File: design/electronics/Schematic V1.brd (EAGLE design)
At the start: 152.4 x 139.7 mm, 180 parts, among them J1 PJ-202AH, J2 PJ-025, J3 DD50P564GTXLF, J4 DD50P564GTXLF, J5 SAMTEC-TST-105-01-X-DJ, J6 SSW-106-02-TM-S-RA, SW1 TL6330AF200Q, U1 STM32F207VGT6TR, U10 SN65LBC175ADD16-M, U11 MAX7375AXR805+T21-0075D_MXM-M, U12 SN75ALS174ADWRDW20-M, U13 SN75468DRD0016A_M, U14 SN75468DRD0016A_M, U15 ACSL-6400-00TESOIC_6400-00TE-M, U16 ACSL-6400-00TESOIC_6400-00TE-M, U17 SN65LBC175ADD16-M, U18 SN65LBC175ADD16-M, U19 SN65LBC175ADD16-M, U2 LM2678S-5.0/NOPBTS7B-M, U21 RS0104YQTSSOP-14_JRT-M, U22 RS0104YQTSSOP-14_JRT-M, U24 RS0104YQTSSOP-14_JRT-M, U3 CDBC520-GCDBC-G-M, U4 TLV1117LV33DCYR, U5 LM43601PWPRPWP16_TEX-M, U6 RS0104YQTSSOP-14_JRT-M, U7 SN75ALS174ADWRDW20-M, U8 OPA4205APWRTSSOP14_PW_R-PDSO-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

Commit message: Yay it's hooked up
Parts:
- added R75: 33k, rcl:R0805
- added R76: 66k, rcl:R0805
- moved LED3 143.4 mm to (42.5, 54.6), turned to 270 degrees
- moved LED4 113.1 mm to (3.81, 66.0), turned to 180 degrees
- moved TP5 106.0 mm to (50.8, 130.8)
- moved TP6 97.8 mm to (58.4, 69.8)
- moved TP4 90.9 mm to (34.3, 130.8)
- moved TP3 86.0 mm to (50.8, 47.0)
- moved TP2 67.5 mm to (37.5, 60.7)
- moved R21 58.0 mm to (41.5, 58.4), turned to 270 degrees
- moved R22 29.0 mm to (3.81, 71.1), turned to 270 degrees
- moved R73 0.28 mm to (68.1, 105.4)
- moved C53 0.28 mm to (115.4, 25.1)
- renumbered U10 to LINE_RECEIVER, U13 to NPN, U15 to OPTOCOUPLER, U21 to LEVEL_SHIFTER
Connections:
- removed net V_ON_5V: U12.15
- new net V_ON_5V_6: R75.1, R76.2, U12.15
- net +5V: now also R75.2
- net S_GND: now also R76.1
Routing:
- net TORQUE-SPEED_ANALOG_2: track 8.11 -> 149.9 mm, vias 1 -> 7
- net P_GND: track 231.1 -> 319.1 mm, vias 19 -> 27
- net S_GND: track 495.2 -> 513.9 mm, vias 34 -> 36
- net +5V: track 320.8 -> 333.8 mm, vias 21 -> 24
- net +3.3V: track 227.5 -> 238.7 mm, vias 19 -> 21
- net V_ON_5V_6: track 0.00 -> 9.01 mm, vias 0 -> 1
- net N$30: track 0.00 -> 3.08 mm
- net N$24: track 0.00 -> 2.85 mm
- net SERVO_ALARM_OUT_LO_1: track 32.3 -> 34.5 mm
- net +24V: track 447.8 -> 449.5 mm
- net ALO_GPIO_A_1: track 17.1 -> 15.5 mm
- net V_ON_14V: track 6.39 -> 7.86 mm
- net ENC_PUL_OUT_C_LO_2: track 31.7 -> 30.9 mm
- net CLR_LO_2: track 92.5 -> 93.3 mm
- net ALO_GPIO_C_2: track 36.4 -> 35.7 mm
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
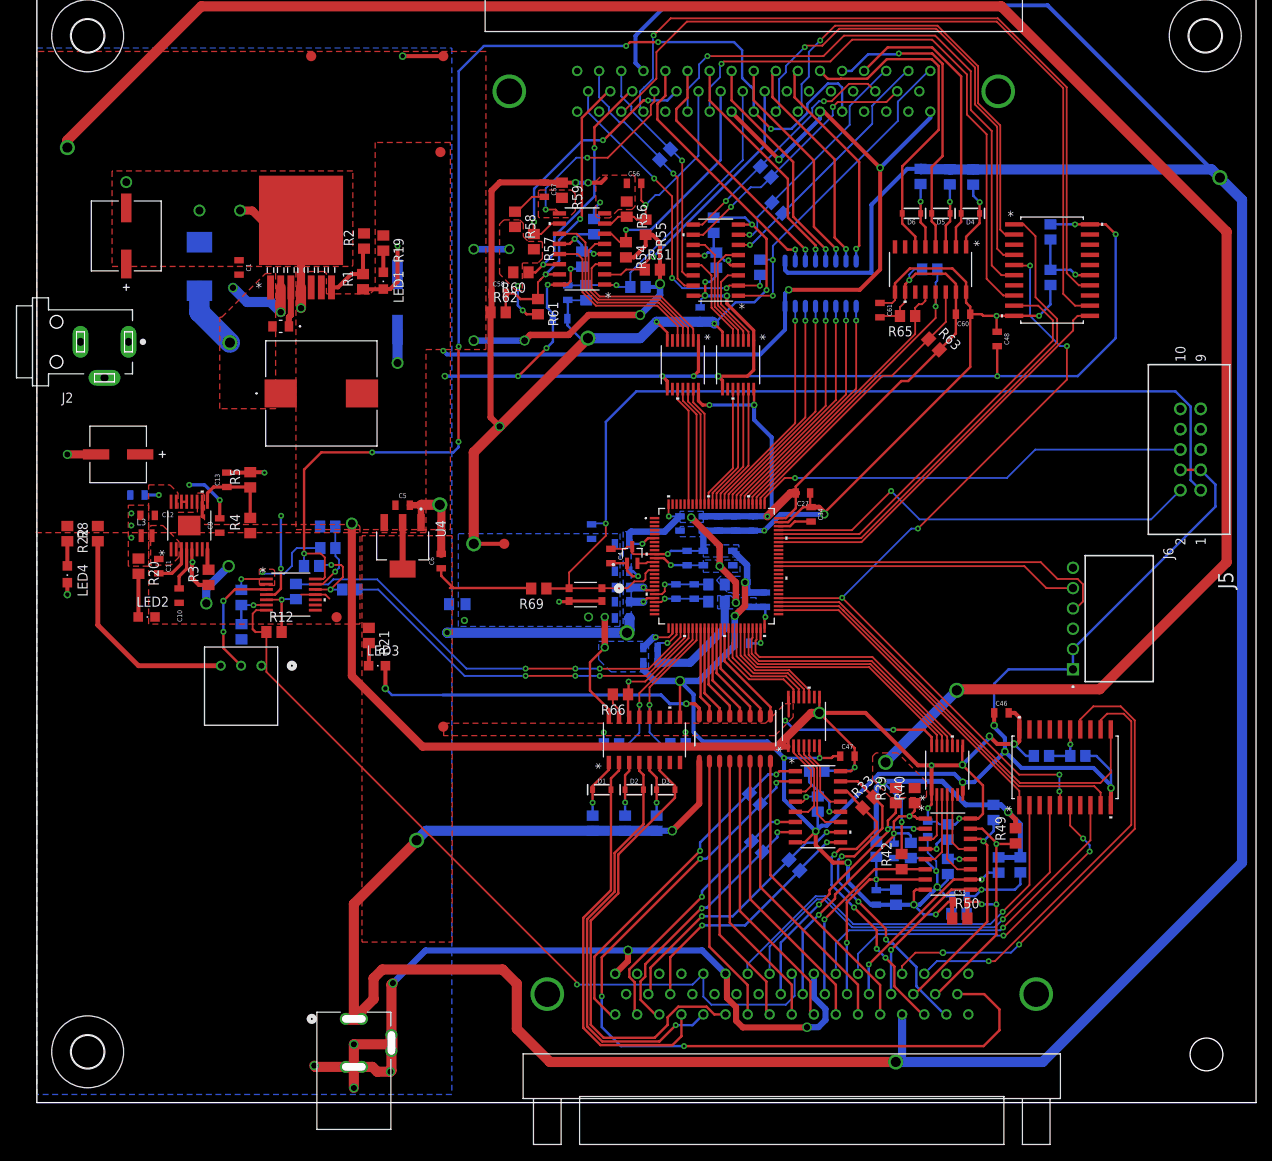
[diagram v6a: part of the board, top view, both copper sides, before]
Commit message: Updated part library of barrel jack + stretched polygons
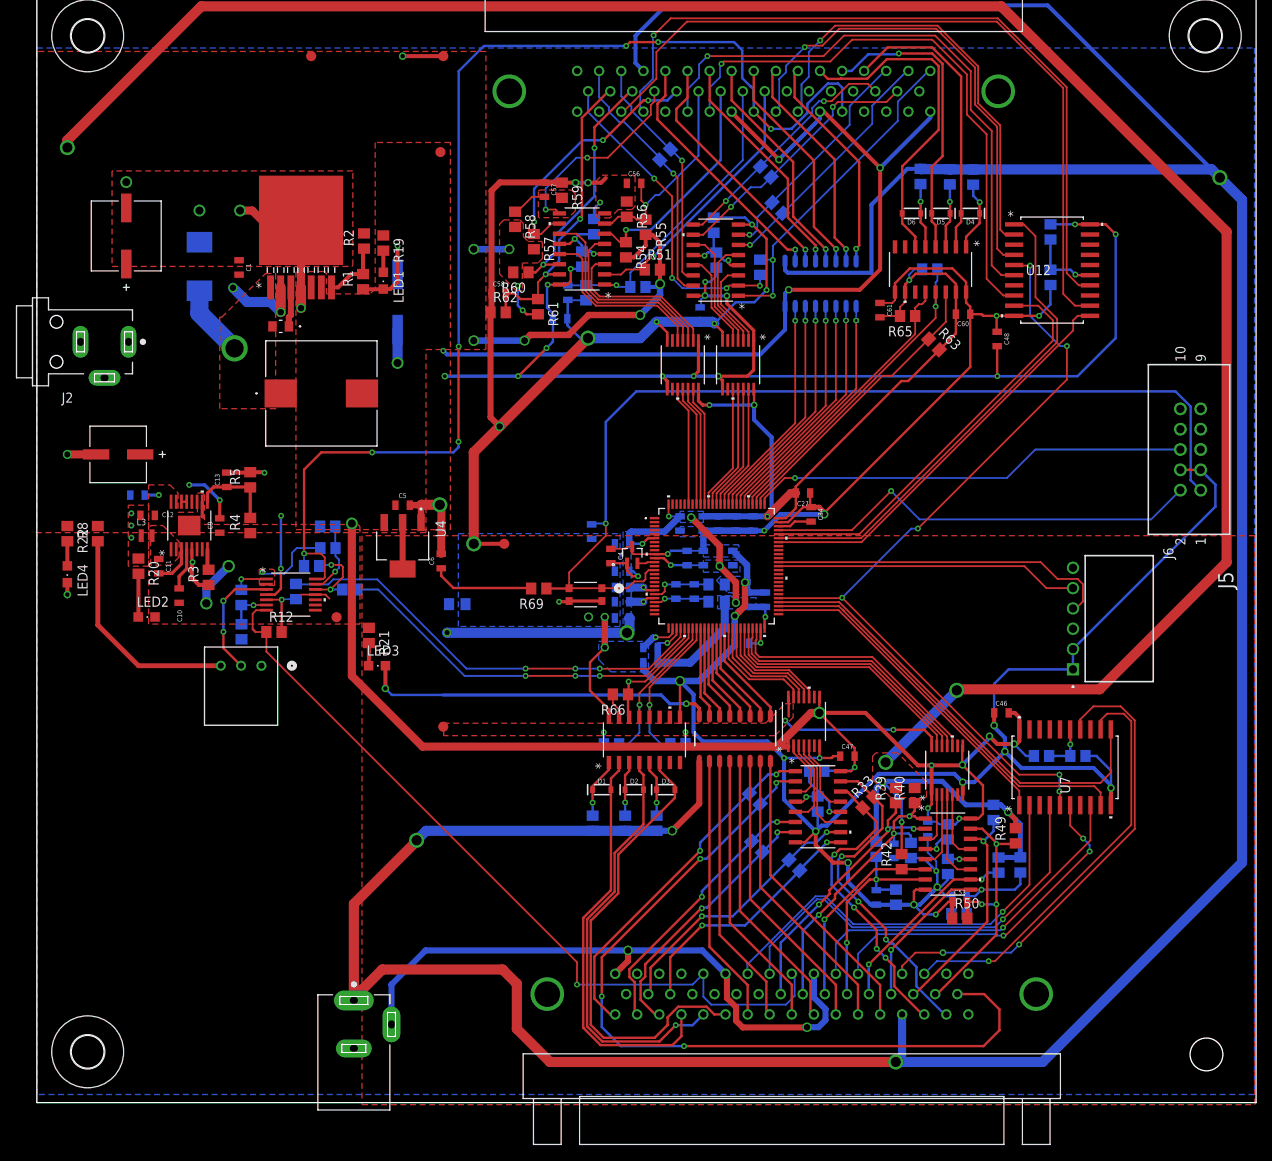
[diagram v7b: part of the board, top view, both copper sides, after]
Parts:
- J1: device SSW-130-01-G-S:CONN3_PJ-202_CUD -> SSW-130-01-G-S:CUI_PJ-202AH
- moved J1 4.19 mm to (39.6, 6.27), turned to 270 degrees
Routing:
- net P_GND: track 319.1 -> 291.9 mm, vias 27 -> 22
- net +24V: track 449.5 -> 444.8 mm
- net SWITCH_OUT_5V: track 8.07 -> 9.02 mm
- net S_GND: vias 36 -> 35
